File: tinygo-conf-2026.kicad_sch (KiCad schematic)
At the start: 15 parts, among them J1 Conn_01x04_Pin, J2 Conn_01x03_Pin, J3 Conn_01x08_Pin, SW1 SW_Push, SW2 SW_Push, U2 RKJXV122400R, U3 adafruit-MAX98357

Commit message: フットプリントライブラリとシンボルのファイル追加と更新
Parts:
- removed U1: ~, espressif:ESP32-S3-DevKitC_ZigZag, symbol kbd:ESP32-S3-Devkit
- added U4: ESP32-S3-Devkit, origin:ESP32-S3-DevKitC_ZigZag, symbol esp32-devkit:ESP32-S3-Devkit
- J3: footprint ST7789:ST7789_1.3_240x240_LCD_Module_Zigzag -> ST7789:ST7789_1.3_240x240_LCD_Module
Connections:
- net 3V3: now also U4.1 (3V3), U4.2 (3V3)
- net BCLK: now also U4.30 (GPIO45)
- net CS: now also U4.16 (GPIO10)
- net DC: now also U4.5 (GPIO5)
- net DIN: now also U4.28 (GPIO47)
- net GND: now also U4.22 (GND), U4.23 (GND), U4.24 (GND)
- net I2C_SCL: now also U4.15 (GPIO9)
- net I2C_SDA: now also U4.12 (GPIO8)
- net IR_DATA: now also U4.11 (GPIO18)
- net IR_LED: now also U4.10 (GPIO17)
- net LED: now also U4.9 (GPIO16)
- net LRC: now also U4.29 (GPIO48)
- net RES: now also U4.4 (GPIO4)
- net SCL: now also U4.18 (GPIO12)
- net SDA: now also U4.17 (GPIO11)
- net SW1: now also U4.19 (GPIO13)
- net SW2: now also U4.20 (GPIO14)
- net VCC: now also U4.21 (5V)
- net VR_BTN: now also U4.8 (GPIO15)
- net VR_X: now also U4.7 (GPIO7)
- net VR_Y: now also U4.6 (GPIO6)
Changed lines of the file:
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@@
+	)
+	(symbol
+		(lib_id "esp32-devkit:ESP32-S3-Devkit")
+		(at 90.17 40.64 0)
+		(unit 1)
+		(exclude_from_sim no)
+		(in_bom yes)
+		(on_board yes)
+		(dnp no)
+		(fields_autoplaced yes)
+		(property "Reference" "U4"
+			(at 99.695 38.1 0)
+			(effects
+				(font
+					(size 1.27 1.27)
+				)
+			)
+		)
+		(property "Value" "ESP32-S3-Devkit"
+			(at 99.695 40.64 0)
+			(effects
+				(font
+					(size 1.27 1.27)
+				)
+			)
+		)
+		(property "Footprint" "origin:ESP32-S3-DevKitC_ZigZag"
+			(at 90.17 40.64 0)
+			(effects
+				(font
+					(size 1.27 1.27)
+				)
+				(hide yes)
+			)
+		)
+		(property "Datasheet" ""
+			(at 90.17 40.64 0)
+			(effects
+				(font
+					(size 1.27 1.27)
+				)
+				(hide yes)
+			)
+		)
+		(property "Description" ""
+			(at 90.17 40.64 0)
+			(effects
+				(font
+					(size 1.27 1.27)
+				)
+				(hide yes)
+			)
+		)
+		(pin "41"
+		)
+		(pin "32"
+		)
+		(pin "26"
+		)
+		(pin "5"
+		)
+		(pin "4"
+		)
+		(pin "7"
+		)
+		(pin "3"
+		)
+		(pin "39"
+		)
+		(pin "35"
+		)
+		(pin "38"
+		)
+		(pin "18"
+		)
+		(pin "12"
+		)
+		(pin "29"
+		)
+		(pin "22"
+		)
+		(pin "21"
+		)
+		(pin "44"
+		)
+		(pin "20"
+		)
+		(pin "42"
+		)
+		(pin "43"
+		)
+		(pin "31"
+		)
+		(pin "10"
+		)
+		(pin "37"
+		)
+		(pin "33"
+		)
+		(pin "40"
+		)
+		(pin "30"
+		)
+		(pin "36"
+		)
+		(pin "34"
+		)
+		(pin "23"
+		)
+		(pin "24"
+		)
+		(pin "15"
+		)
+		(pin "13"
+		)
+		(pin "25"
+		)
+		(pin "2"
+		)
+		(pin "17"
+		)
+		(pin "19"
+		)
+		(pin "9"
+		)
+		(pin "6"
+		)
+		(pin "14"
+		)
+		(pin "28"
+		)
+		(pin "8"
+		)
+		(pin "1"
+		)
+		(pin "27"
+		)
+		(pin "16"
+		)
+		(pin "11"
+		)
+		(instances
+			(project "tinygo-conf-2026"
+				(path "/29db373d-5a3f-48db-987c-83fa700d9f95"
+					(reference "U4")
+					(unit 1)
+				)
+			)
+		)
 	)
 	(symbol
@@
 			)
 		)
-		(property "Footprint" "ST7789:ST7789_1.3_240x240_LCD_Module_Zigzag"
+		(property "Footprint" "ST7789:ST7789_1.3_240x240_LCD_Module"
 			(at 144.78 125.73 0)
 			(effects
@@
 					(unit 1)
 				)
-			)
-		)
-	)
-	(symbol
-		(lib_id "kbd:ESP32-S3-Devkit")
-		(at 90.17 40.64 0)
-		(unit 1)
-		(exclude_from_sim no)
-		(in_bom yes)
-		(on_board yes)
-		(dnp no)
-		(fields_autoplaced yes)
-		(property "Reference" "U1"
-			(at 99.695 38.1 0)
-			(effects
-				(font
-					(size 1.27 1.27)
-				)
-			)
-		)
-		(property "Value" "~"
-			(at 99.695 40.64 0)
-			(effects
-				(font
-					(size 1.27 1.27)
-				)
-			)
-		)
-		(property "Footprint" "espressif:ESP32-S3-DevKitC_ZigZag"
-			(at 90.17 40.64 0)
-			(effects
-				(font
-					(size 1.27 1.27)
-				)
-				(hide yes)
-			)
-		)
-		(property "Datasheet" ""
-			(at 90.17 40.64 0)
-			(effects
-				(font
-					(size 1.27 1.27)
-				)
-				(hide yes)
-			)
-		)
-		(property "Description" ""
-			(at 90.17 40.64 0)
-			(effects
-				(font
-					(size 1.27 1.27)
-				)
-				(hide yes)
-			)
-		)
-		(pin "24"
-		)
-		(pin "23"
-		)
-		(pin "37"
-		)
-		(pin "43"
-		)
-		(pin "19"
-		)
-		(pin "38"
-		)
-		(pin "29"
-		)
-		(pin "32"
-		)
-		(pin "41"
-		)
-		(pin "2"
-		)
-		(pin "5"
-		)
-		(pin "42"
-		)
-		(pin "21"
-		)
-		(pin "31"
-		)
-		(pin "11"
-		)
-		(pin "8"
-		)
-		(pin "25"
-		)
-		(pin "4"
-		)
-		(pin "3"
-		)
-		(pin "34"
-		)
-		(pin "30"
-		)
-		(pin "18"
-		)
-		(pin "26"
-		)
-		(pin "7"
-		)
-		(pin "35"
-		)
-		(pin "28"
-		)
-		(pin "15"
-		)
-		(pin "27"
-		)
-		(pin "44"
-		)
-		(pin "16"
-		)
-		(pin "13"
-		)
-		(pin "9"
-		)
-		(pin "33"
-		)
-		(pin "10"
-		)
-		(pin "40"
-		)
-		(pin "20"
-		)
-		(pin "14"
-		)
-		(pin "6"
-		)
-		(pin "22"
-		)
-		(pin "36"
-		)
-		(pin "17"
-		)
-		(pin "39"
-		)
-		(pin "1"
-		)
-		(pin "12"
-		)
-		(instances
-			(project "tinygo-conf-2026"
-				(path "/29db373d-5a3f-48db-987c-83fa700d9f95"
-					(reference "U1")
-					(unit 1)
-				)

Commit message: ファイルを追加してリネーム
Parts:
- added J4: AHT21B, Connector_PinHeader_2.54mm:PinHeader_1x04_P2.54mm_Vertical, symbol Connector:Conn_01x04_Pin
- added J5: Conn_02x08_Counter_Clockwise, Connector_PinSocket_2.54mm:PinSocket_2x08_P2.54mm_Vertical, symbol Connector_Generic:Conn_02x08_Counter_Clockwise
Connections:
- net 3V3: now also J4.1 (Pin_1), J5.1 (Pin_1), J5.2 (Pin_2)
- net GND: now also U4.44 (GND), J4.3 (Pin_3), J5.8 (Pin_8), J5.9 (Pin_9)
- net VCC: now also J5.16 (Pin_16)
- net GPIO3: now reaches U4.13 (GPIO3)
- net GPIO3: now also J5.5 (Pin_5)
- net SCL_AHT21B: now reaches U4.25 (GPIO19)
- net SCL_AHT21B: now also J4.4 (Pin_4)
- net SDA_AHT21B: now reaches U4.26 (GPIO20)
- net SDA_AHT21B: now also J4.2 (Pin_2)
- net GPIO35: now reaches U4.32 (GPIO35)
- net GPIO35: now also J5.6 (Pin_6)
- net GPIO36: now reaches U4.33 (GPIO36)
- net GPIO36: now also J5.7 (Pin_7)
- net GPIO37: now reaches U4.34 (GPIO37)
- net GPIO37: now also J5.10 (Pin_10)
- net GPIO38: now reaches U4.35 (GPIO38)
- net GPIO38: now also J5.11 (Pin_11)
- net GPIO39: now reaches U4.36 (GPIO39/MTCK)
- net GPIO39: now also J5.12 (Pin_12)
- net GPIO40: now reaches U4.37 (GPIO40/MTDO)
- net GPIO40: now also J5.13 (Pin_13)
- net GPIO41: now reaches U4.38 (GPIO41/MTDI)
- net GPIO41: now also J5.14 (Pin_14)
- net GPIO42: now reaches U4.39 (GPIO42/MTMS)
- net GPIO42: now also J5.15 (Pin_15)
- net GPIO2: now reaches U4.40 (GPIO2)
- net GPIO2: now also J5.4 (Pin_4)
- net GPIO1: now reaches U4.41 (GPIO1)
- net GPIO1: now also J5.3 (Pin_3)

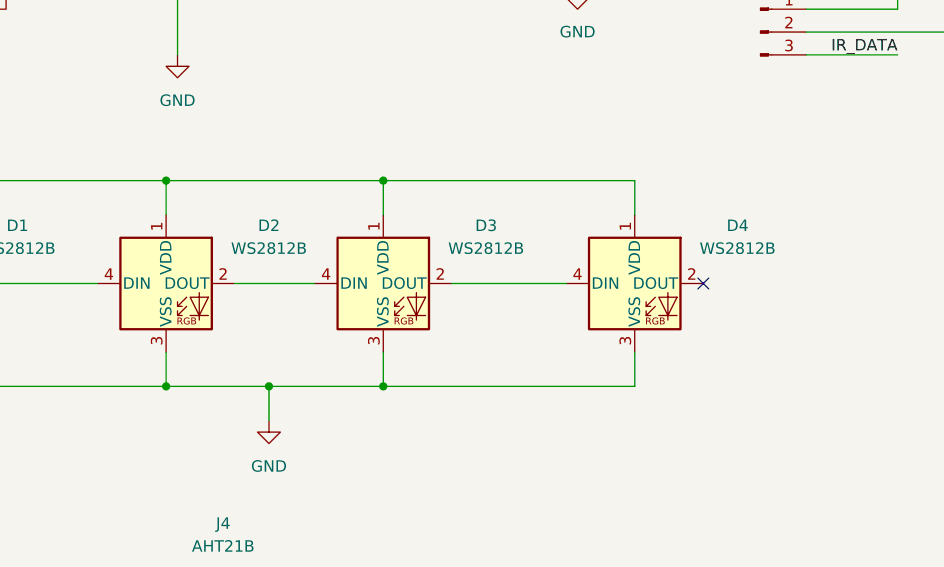
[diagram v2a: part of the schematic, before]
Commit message: 配線変更と基板の穴を追加
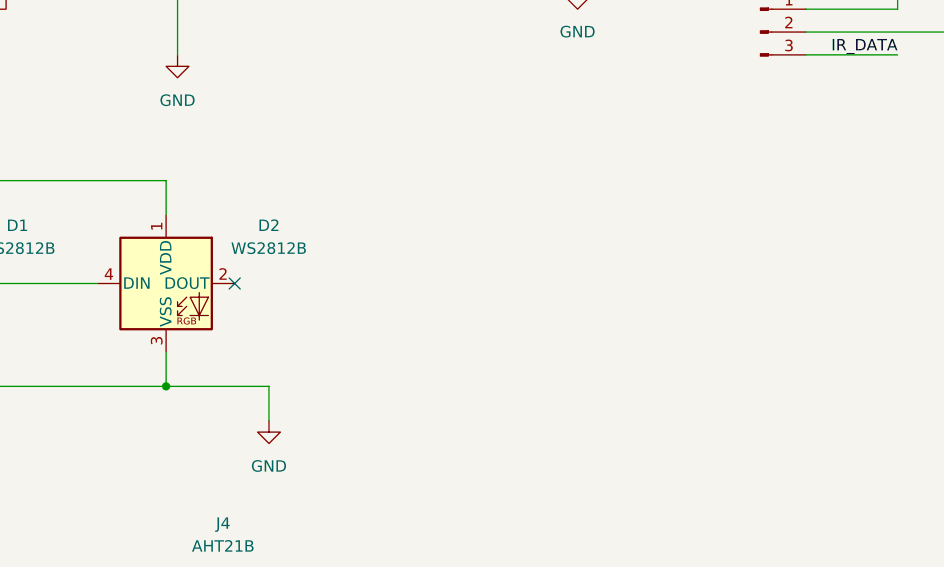
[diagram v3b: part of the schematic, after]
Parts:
- removed D3, D4: WS2812B, kbd:YS-SK6812MINI-E, symbol LED:WS2812B
- U4: footprint origin:ESP32-S3-DevKitC_ZigZag -> espressif:ESP32-S3-DevKitC

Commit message: 温湿度センサーのGPIOがUSBとかぶっていたので変更
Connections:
- net 3V3: now also J2.1 (Pin_1)
- net LRC: now also U4.27 (GPIO21); no longer U4.29 (GPIO48)
- net SCL_AHT21B: now also U4.29 (GPIO48); no longer U4.25 (GPIO19)
- net SDA_AHT21B: now also U4.14 (GPIO46); no longer U4.26 (GPIO20)
- net VCC: no longer J2.1 (Pin_1)
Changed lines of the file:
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@@
 	(wire
 		(pts
+			(xy 130.81 44.45) (xy 130.81 48.26)
+		)
+		(stroke
+			(width 0)
+			(type default)
+		)
+	)
+	(wire
+		(pts
 			(xy 25.4 58.42) (xy 34.29 58.42)
 		)
@@
 	(wire
 		(pts
-			(xy 124.46 44.45) (xy 124.46 46.99)
-		)
-		(stroke
-			(width 0)
-			(type default)
-		)
-	)
-	(wire
-		(pts
 			(xy 46.99 48.26) (xy 55.88 48.26)
 		)
@@
 	(wire
 		(pts
-			(xy 115.57 92.71) (xy 129.54 92.71)
+			(xy 115.57 82.55) (xy 129.54 82.55)
 		)
 		(stroke
@@
 	(wire
 		(pts
-			(xy 115.57 44.45) (xy 124.46 44.45)
+			(xy 115.57 44.45) (xy 130.81 44.45)
 		)
 		(stroke
@@
 	(wire
 		(pts
-			(xy 115.57 90.17) (xy 129.54 90.17)
+			(xy 69.85 77.47) (xy 83.82 77.47)
 		)
 		(stroke
@@
 	(wire
 		(pts
-			(xy 115.57 82.55) (xy 123.19 82.55)
+			(xy 115.57 87.63) (xy 123.19 87.63)
 		)
 		(stroke
@@
 	)
 	(label "SCL_AHT21B"
-		(at 129.54 92.71 180)
+		(at 129.54 82.55 180)
 		(effects
 			(font
@@
 	)
 	(label "LRC"
-		(at 123.19 82.55 180)
+		(at 123.19 87.63 180)
 		(effects
 			(font
@@
 	)
 	(label "SDA_AHT21B"
-		(at 129.54 90.17 180)
+		(at 69.85 77.47 0)
 		(effects
 			(font
 				(size 1.27 1.27)
 			)
-			(justify right bottom)
+			(justify left bottom)
 		)
 	)
@@
 		)
 	)
+	(label "3V3"
+		(at 261.62 58.42 180)
+		(effects
+			(font
+				(size 1.27 1.27)
+			)
+			(justify right bottom)
+		)
+	)
 	(label "DIN"
 		(at 123.19 85.09 180)
@@
 	(symbol
 		(lib_id "power:GND")
-		(at 124.46 46.99 0)
+		(at 130.81 48.26 0)
 		(unit 1)
 		(exclude_from_sim no)
@@
 		(fields_autoplaced yes)
 		(property "Reference" "#PWR014"
-			(at 124.46 53.34 0)
+			(at 130.81 54.61 0)
 			(effects
 				(font
@@
 		)
 		(property "Value" "GND"
-			(at 124.46 52.07 0)
+			(at 130.81 53.34 0)
 			(effects
 				(font
@@
 		)
 		(property "Footprint" ""
-			(at 124.46 46.99 0)
+			(at 130.81 48.26 0)
 			(effects
 				(font
@@
 		)
 		(property "Datasheet" ""
-			(at 124.46 46.99 0)
+			(at 130.81 48.26 0)
 			(effects
 				(font
@@
 		)
 		(property "Description" "Power symbol creates a global label with name \"GND\" , ground"
-			(at 124.46 46.99 0)
+			(at 130.81 48.26 0)
 			(effects
 				(font
@@
 					(unit 1)
 				)
-			)
-		)
-	)
-	(symbol
-		(lib_id "power:VCC")
-		(at 261.62 58.42 0)
-		(unit 1)
-		(exclude_from_sim no)
-		(in_bom yes)
-		(on_board yes)
-		(dnp no)
-		(fields_autoplaced yes)
-		(property "Reference" "#PWR012"
-			(at 261.62 62.23 0)
-			(effects
-				(font
-					(size 1.27 1.27)
-				)
-				(hide yes)
-			)
-		)
-		(property "Value" "VCC"
-			(at 261.62 53.34 0)
-			(effects
-				(font
-					(size 1.27 1.27)
-				)
-			)
-		)
-		(property "Footprint" ""
-			(at 261.62 58.42 0)
-			(effects
-				(font
-					(size 1.27 1.27)
-				)
-				(hide yes)
-			)
-		)
-		(property "Datasheet" ""
-			(at 261.62 58.42 0)
-			(effects
-				(font
-					(size 1.27 1.27)
-				)
-				(hide yes)
-			)
-		)
-		(property "Description" "Power symbol creates a global label with name \"VCC\""
-			(at 261.62 58.42 0)
-			(effects
-				(font
-					(size 1.27 1.27)
-				)
-				(hide yes)
-			)
-		)
-		(pin "1"
-		)
-		(instances
-			(project "tinygo-conf-2026"
-				(path "/29db373d-5a3f-48db-987c-83fa700d9f95"
-					(reference "#PWR012")
-					(unit 1)
-				)

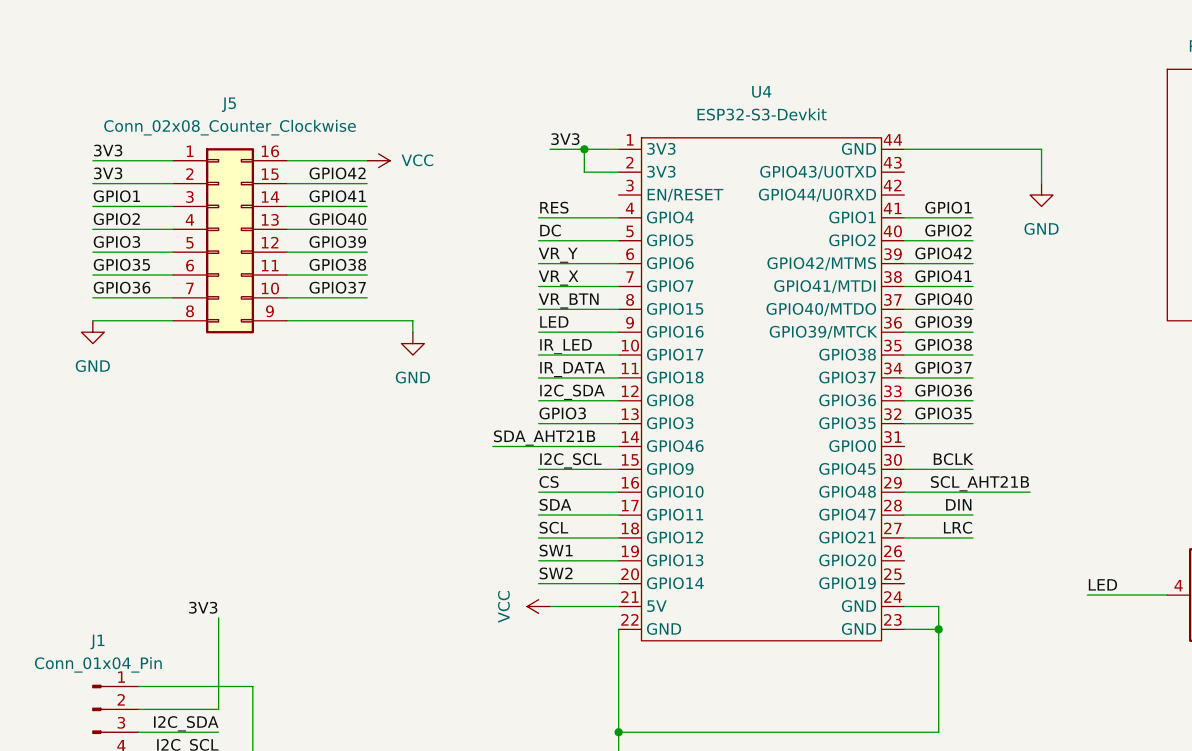
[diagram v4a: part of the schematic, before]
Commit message: PSRAM用のGPIOを使わないように再配線
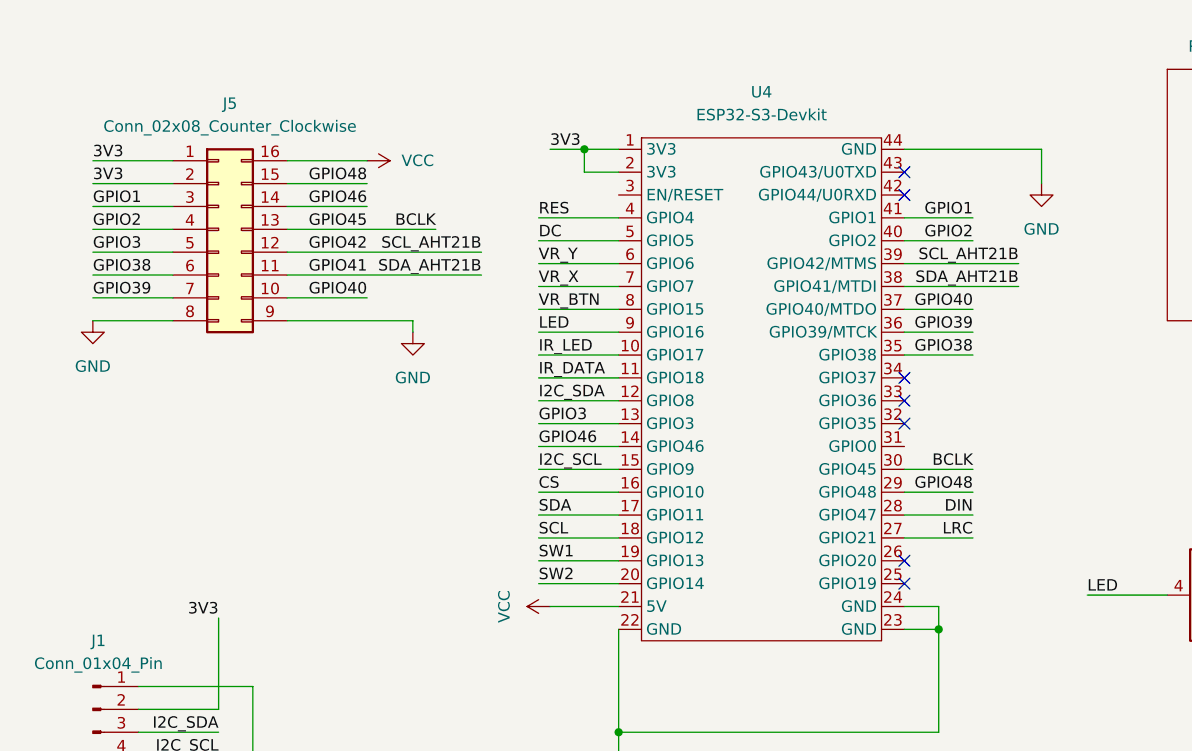
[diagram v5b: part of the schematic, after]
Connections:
- net BCLK: now also J5.13 (Pin_13)
- net GPIO38: now also J5.6 (Pin_6); no longer J5.11 (Pin_11)
- net GPIO39: now also J5.7 (Pin_7); no longer J5.12 (Pin_12)
- net GPIO40: now also J5.10 (Pin_10); no longer J5.13 (Pin_13)
- net GPIO41: now also J4.2 (Pin_2), J5.11 (Pin_11); no longer J5.14 (Pin_14)
- net GPIO42: now also J4.4 (Pin_4), J5.12 (Pin_12); no longer J5.15 (Pin_15)
- net GPIO35: no longer names the net of U4.32 (GPIO35)
- net GPIO35: no longer J5.6 (Pin_6)
- net GPIO36: no longer names the net of U4.33 (GPIO36)
- net GPIO36: no longer J5.7 (Pin_7)
- net GPIO37: no longer names the net of U4.34 (GPIO37)
- net GPIO37: no longer J5.10 (Pin_10)
- net SCL_AHT21B renamed GPIO48
- net GPIO48: now also J5.15 (Pin_15); no longer J4.4 (Pin_4)
- net SDA_AHT21B renamed GPIO46
- net GPIO46: now also J5.14 (Pin_14); no longer J4.2 (Pin_2)
- no-connect marks 2 -> 9
